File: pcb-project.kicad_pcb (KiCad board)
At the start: 2 copper layers, 110 x 60 mm, 62 parts, among them J1 Conn_01x03, J2 USB_C_Receptacle_USB2.0_16P, J3 Conn_01x14, J4 Conn_01x02, J5 Conn_01x05, J6 Conn_01x06, Q1 MMBT2222A, SW1 SW_Push, SW10 SW_Push, SW2 SW_Push, SW3 SW_Push, SW4 SW_Push, SW5 SW_Push, SW6 SW_Push, SW7 SW_Push, SW8 SW_Push, SW9 SW_Push, U1 RP2040, U2 W25Q128JVS, U3 AP2112K-3.3, U4 PAM8302AAD, Y1 12MHz

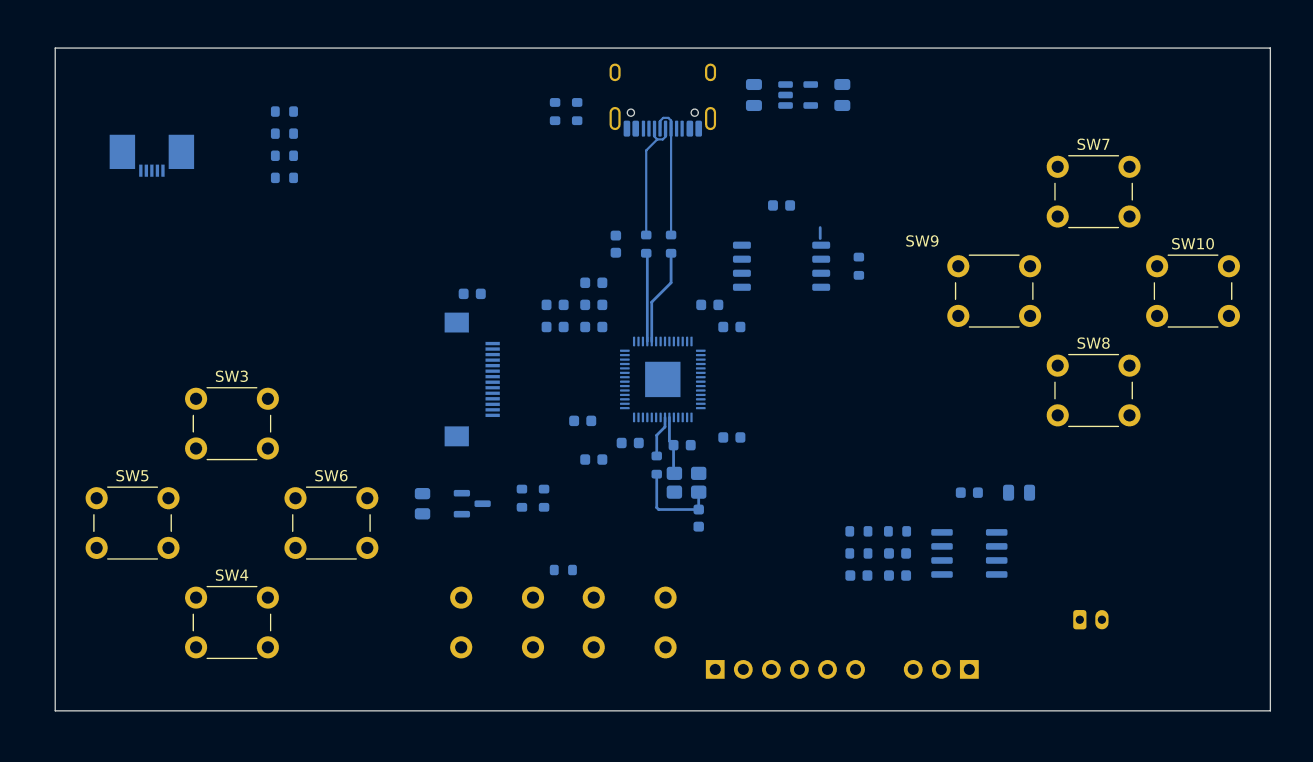
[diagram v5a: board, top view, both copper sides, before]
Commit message: handrouted wires, 14 unrouted
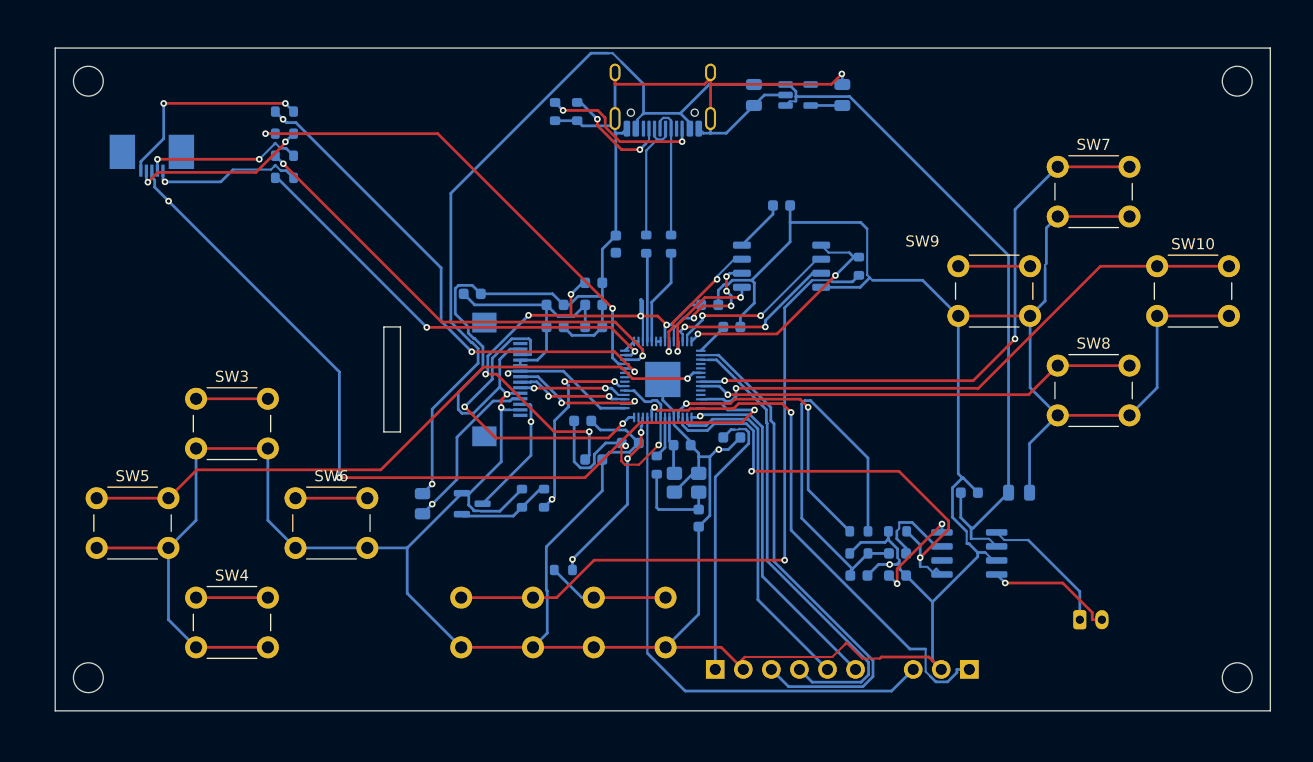
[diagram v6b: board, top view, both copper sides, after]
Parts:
- moved J3 2.50 mm to (143.5, 82.2)
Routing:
- net GND: track 0.00 -> 483.9 mm, vias 0 -> 5
- net VBUS: track 0.00 -> 135.9 mm, vias 0 -> 1
- net +3V3: track 0.00 -> 83.0 mm, vias 0 -> 2
- net /STICK_SW: track 0.00 -> 80.0 mm, vias 0 -> 3
- net Net-(R2-Pad1): track 0.00 -> 61.6 mm, vias 0 -> 1
- net Net-(U1-GPIO4): track 0.00 -> 60.3 mm, vias 0 -> 1
- net Net-(U1-GPIO6): track 0.00 -> 53.7 mm, vias 0 -> 2
- net Net-(U1-GPIO9): track 0.00 -> 53.4 mm, vias 0 -> 1
- net +1V1: track 0.00 -> 48.5 mm, vias 0 -> 6
- net Net-(J1-Pin_1): track 0.00 -> 48.4 mm, vias 0 -> 2
- net Net-(J1-Pin_3): track 0.00 -> 47.6 mm
- net Net-(J6-Pin_3): track 0.00 -> 46.7 mm
- net Net-(U1-GPIO26/ADC0): track 0.00 -> 46.1 mm, vias 0 -> 3
- net Net-(U1-GPIO27/ADC1): track 0.00 -> 44.7 mm, vias 0 -> 2
- net Net-(U1-GPIO28/ADC2): track 0.00 -> 42.9 mm, vias 0 -> 2
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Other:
- outline, holes or cut-outs redrawn

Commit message: handrouted wires, 0 unrouted!!
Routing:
- net +3V3: track 83.0 -> 377.2 mm, vias 2 -> 19
- net Net-(U1-GPIO2): track 6.50 -> 104.8 mm, vias 0 -> 7
- net Net-(U1-GPIO5): track 6.50 -> 88.0 mm, vias 0 -> 6
- net Net-(U1-GPIO3): track 6.50 -> 63.3 mm, vias 0 -> 8
- net Net-(U1-GPIO8): track 6.50 -> 40.2 mm, vias 0 -> 2
- net +1V1: track 48.5 -> 77.3 mm, vias 6 -> 13
- net GND: track 483.9 -> 485.2 mm
- net Net-(J1-Pin_1): track 48.4 -> 49.4 mm

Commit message: Add board pictures, gerbers and final layout
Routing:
- added copper zone on B.Cu, net GND
- added copper zone on F.Cu, net GND
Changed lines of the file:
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@@
 			(plot_on_all_layers_selection 0x00000000_00000000_00000000_00000000)
 			(disableapertmacros no)
-			(usegerberextensions no)
+			(usegerberextensions yes)
 			(usegerberattributes yes)
 			(usegerberadvancedattributes yes)
@@
 			(outputformat 1)
 			(mirror no)
-			(drillshape 1)
+			(drillshape 0)
 			(scaleselection 1)
-			(outputdirectory "")
+			(outputdirectory "gerbers/")
 		)
 	)
@@
 		(net "Net-(J4-Pin_2)")
 	)
+	(zone
+		(net "GND")
+		(layers "F.Cu" "B.Cu")
+		(hatch edge 0.5)
+		(connect_pads yes
+			(clearance 0.5)
+		)
+		(min_thickness 0.25)
+		(fill yes
+			(thermal_gap 0.5)
+			(thermal_bridge_width 0.5)
+			(island_removal_mode 0)
+		)
+		(polygon
+			(pts
+				(xy 102.15 50.15) (xy 214.85 51.15) (xy 215.1 114.85) (xy 100.25 114.1) (xy 102 49.9)
+			)
+		)
+	)
 	(embedded_fonts no)
